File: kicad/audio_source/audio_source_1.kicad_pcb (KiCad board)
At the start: 2 copper layers, 20.9 x 20.9 mm, 3 parts, among them J1 SCJ368R1NUS0B00G, P1 IN, P2 OUT

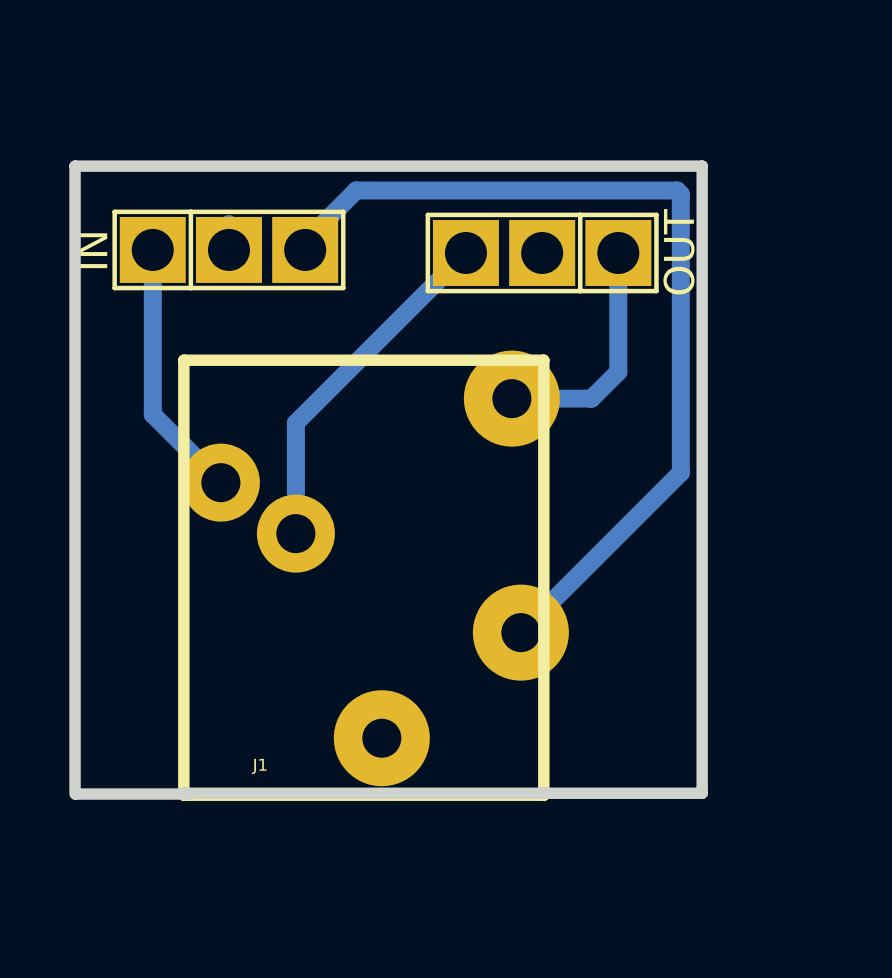
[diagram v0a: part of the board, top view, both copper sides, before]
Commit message: jack update to scj-0354-5PU module
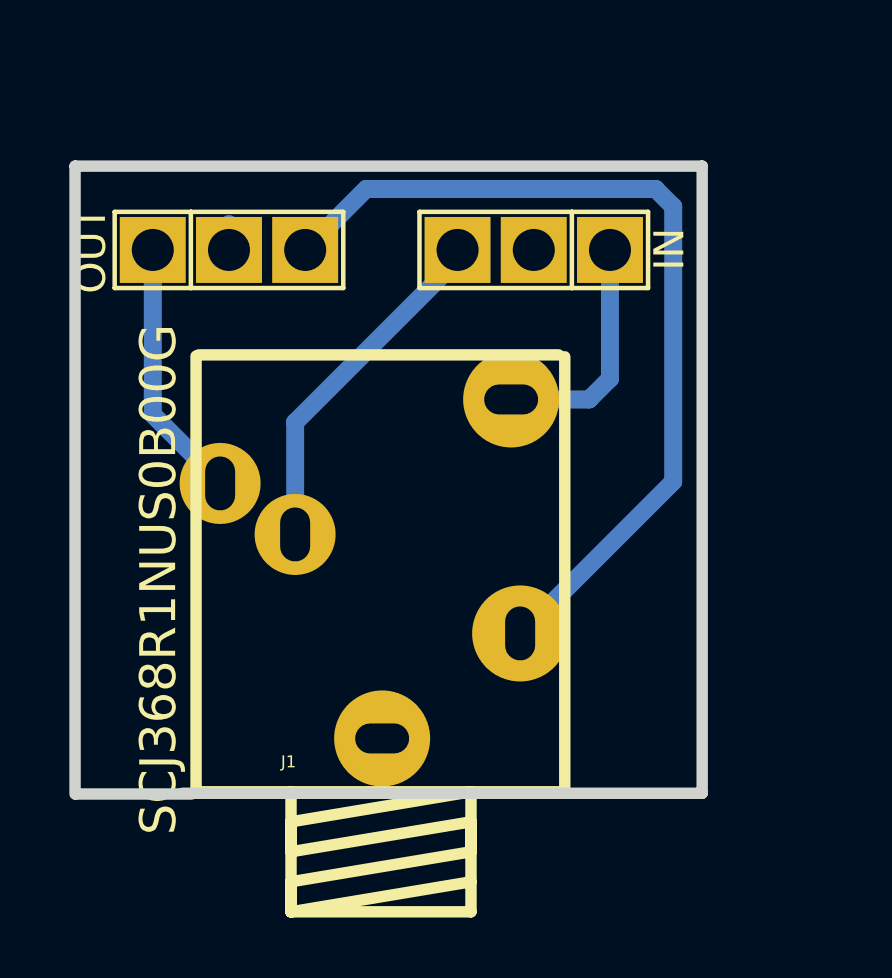
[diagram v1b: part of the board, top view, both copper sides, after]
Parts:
- J1: footprint my_modules:3.5mm_stereo_jack_hacked -> jacks:SCJ-0354-5PU
- moved P2 10.4 mm to (107.4, 92.7), turned to 0 degrees
- moved P1 10.2 mm to (117.6, 92.7), turned to 180 degrees
- moved J1 1.73 mm to (112.5, 110.7)
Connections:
- J1 pad 2: CD_right_in -> RADIO_right_out
- J1 pad 3: RADIO_right_out -> CD_right_in
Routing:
- net CD_right_in: track 30.4 -> 11.7 mm
- net RADIO_left_out: track 11.7 -> 29.7 mm
- net RADIO_right_out: track 8.10 -> 8.71 mm
- net CD_left_in: track 8.70 -> 8.09 mm

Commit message: audio source board update
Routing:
- net RADIO_left_out: track 29.7 -> 15.8 mm
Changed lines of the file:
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@@
-(kicad_pcb (version 4) (host pcbnew 0.201502050101+5404~21~ubuntu14.04.1-product)
+(kicad_pcb (version 4) (host pcbnew 0.201510150733+6269~30~ubuntu14.04.1-product)
   (general
     (links 6)
     (no_connects 0)
-    (area 102.069899 89.725499 123.355101 111.036101)
+    (area 101.6148 80.772 175.006001 115.645973)
     (thickness 1.6002)
     (drawings 7)
-    (tracks 17)
+    (tracks 15)
     (zones 0)
     (modules 3)
@@
   )
   (layers
-    (0 Front signal hide)
+    (0 Front signal)
     (31 Back signal)
     (32 B.Adhes user)
@@
   (gr_line (start 105.8418 110.8202) (end 123.1646 110.8202) (angle 90) (layer Edge.Cuts) (width 0.381))
   (segment (start 107.3912 92.71) (end 107.3912 91.8464) (width 0.59944) (layer Back) (net 1))
-  (segment (start 116.7966 97.6932) (end 119.4006 97.6932) (width 0.59944) (layer Back) (net 3) (status 400000))
-  (segment (start 120.0912 97.0026) (end 120.0912 92.71) (width 0.59944) (layer Back) (net 3) (status 800000))
+  (segment (start 116.7966 97.6932) (end 119.4006 97.6932) (width 0.59944) (layer Back) (net 3))
+  (segment (start 120.0912 97.0026) (end 120.0912 92.71) (width 0.59944) (layer Back) (net 3))
   (segment (start 119.4006 97.6932) (end 120.0912 97.0026) (width 0.59944) (layer Back) (net 3))
   (segment (start 116.6666 97.5106) (end 116.822 97.666) (width 0.59944) (layer Back) (net 3))
+  (segment (start 109.9312 92.71) (end 109.9312 96.139) (width 0.59944) (layer Front) (net 4) (status 400000))
+  (segment (start 117.0966 103.3044) (end 117.0966 105.4932) (width 0.59944) (layer Front) (net 4) (status 800000))
+  (segment (start 109.9312 96.139) (end 117.0966 103.3044) (width 0.59944) (layer Front) (net 4))
   (segment (start 117.0966 105.4932) (end 117.1378 105.4932) (width 0.59944) (layer Back) (net 4))
-  (segment (start 117.1378 105.4932) (end 122.1994 100.4316) (width 0.59944) (layer Back) (net 4))
-  (segment (start 122.1994 100.4316) (end 122.1994 91.2622) (width 0.59944) (layer Back) (net 4))
-  (segment (start 122.1994 91.2622) (end 121.6152 90.678) (width 0.59944) (layer Back) (net 4))
-  (segment (start 121.6152 90.678) (end 111.9632 90.678) (width 0.59944) (layer Back) (net 4))
-  (segment (start 111.9632 90.678) (end 109.9312 92.71) (width 0.59944) (layer Back) (net 4))
-  (segment (start 115.0112 92.71) (end 115.0112 93.0402) (width 0.59944) (layer Back) (net 5) (status C00000))
-  (segment (start 115.0112 93.0402) (end 109.5966 98.4548) (width 0.59944) (layer Back) (net 5) (status 400000))
-  (segment (start 109.5966 98.4548) (end 109.5966 102.1932) (width 0.59944) (layer Back) (net 5) (status 800000))
-  (segment (start 107.0966 100.4932) (end 107.0966 100.4418) (width 0.59944) (layer Back) (net 6) (status C00000))
-  (segment (start 107.0966 100.4418) (end 104.8512 98.1964) (width 0.59944) (layer Back) (net 6) (status 400000))
-  (segment (start 104.8512 98.1964) (end 104.8512 92.71) (width 0.59944) (layer Back) (net 6) (status 800000))
+  (segment (start 115.0112 92.71) (end 115.0112 93.0402) (width 0.59944) (layer Back) (net 5))
+  (segment (start 115.0112 93.0402) (end 109.5966 98.4548) (width 0.59944) (layer Back) (net 5))
+  (segment (start 109.5966 98.4548) (end 109.5966 102.1932) (width 0.59944) (layer Back) (net 5))
+  (segment (start 107.0966 100.4932) (end 107.0966 100.4418) (width 0.59944) (layer Back) (net 6))
+  (segment (start 107.0966 100.4418) (end 104.8512 98.1964) (width 0.59944) (layer Back) (net 6))
+  (segment (start 104.8512 98.1964) (end 104.8512 92.71) (width 0.59944) (layer Back) (net 6))
   (zone (net 2) (net_name GND) (layer Front) (hatch edge 0.508)
     (connect_pads (clearance 0.508))

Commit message: layout update
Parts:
- J1: footprint jacks:SCJ-0354-5PU -> jacks:SCJ-0354-5PU_no_screew
- turned P2 to 180 degrees
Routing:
- net RADIO_left_out: track 15.8 -> 27.5 mm
- removed copper zone on F.Cu, net GND

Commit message: updates
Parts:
- J1: footprint jacks:SCJ-0354-5PU_no_screew -> jacks:3.5mm_stereo_jack_PJ306M_no_screw_terminal
- moved J1 6.51 mm to (112.3, 104.2)
- turned P2 to 0 degrees
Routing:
- net RADIO_left_out: track 27.5 -> 11.1 mm
- net CD_right_in: track 12.1 -> 8.98 mm
- net CD_left_in: track 8.09 -> 10.4 mm
- net RADIO_right_out: track 9.01 -> 7.69 mm
- added copper zone on F.Cu, net AGND
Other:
- board size 20.9 x 20.9 mm -> 18.3 x 15.9 mm
